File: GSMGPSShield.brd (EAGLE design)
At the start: 68.6 x 53.3 mm, 65 parts, among them IC1 RT8289, IC2 SIM900, J1 SIM Socket, J2 Antenna, J3 Breakout 1, J4 Breakout 2, J5 ARDUINO-SHIELD_R3, Q1 2N7002, Q2 2N7002, Q3 2N7002, Q4 2N7002, Q5 2N7002

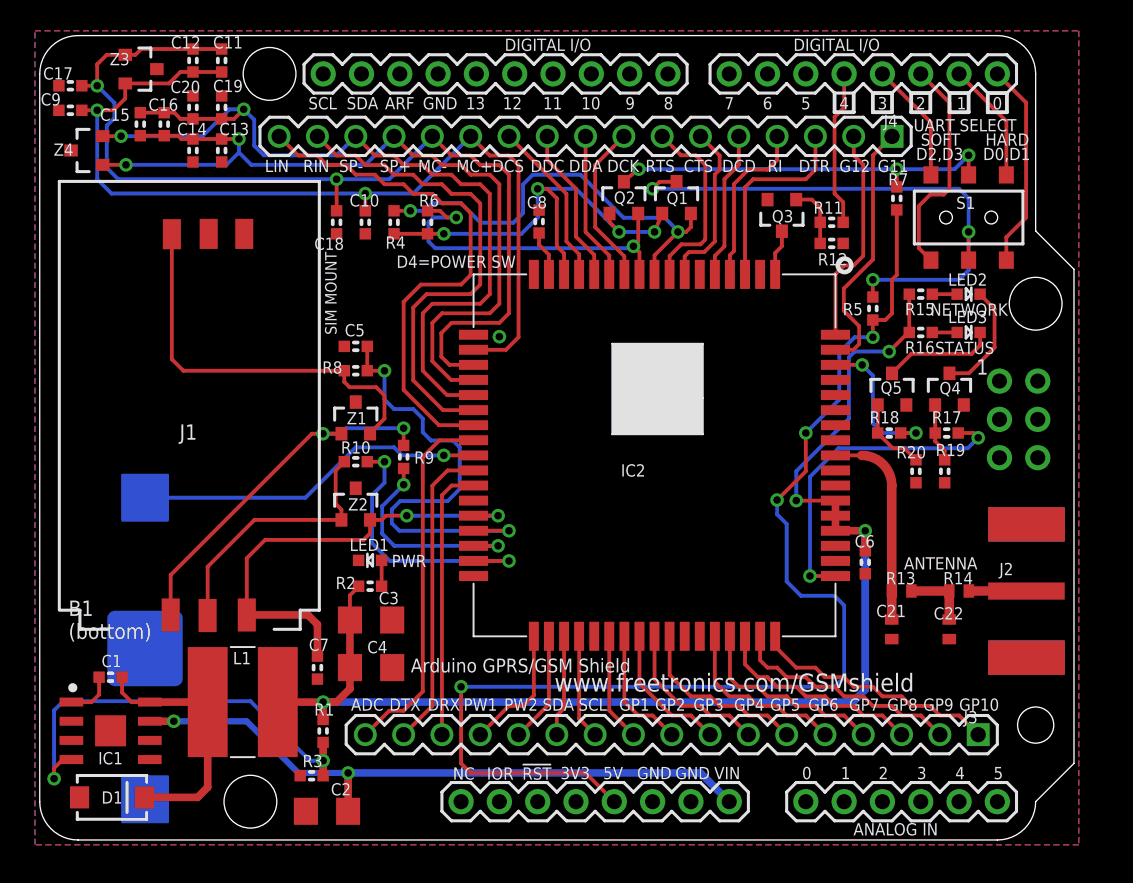
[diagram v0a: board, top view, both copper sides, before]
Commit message: changed to SIM908 module, first finished draft
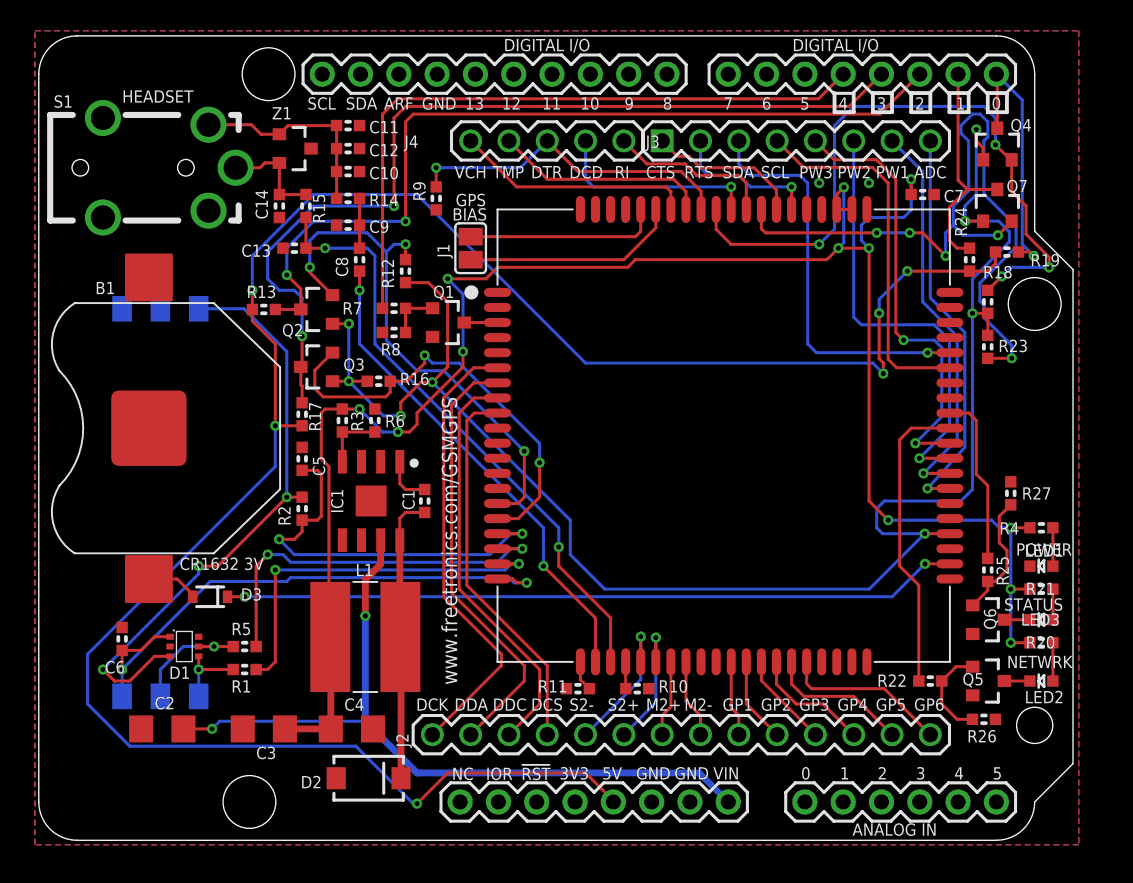
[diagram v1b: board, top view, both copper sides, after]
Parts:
- removed C15, C17, C19: 10pF, freetronics-master-v1:0603
- removed C16, C18, C20: 33pF, freetronics-master-v1:0603
- removed C21, C22: NOT PLACED, freetronics-master-v1:C0402
- removed Z2, Z3, Z4: PGB102ST23, freetronics-luke:SOT23-3
- added D2: B340A-13-F, freetronics-luke:SMA
- added D3: NSR0340HT1G, freetronics-luke:SOD-323
- added IC3: SIM908, freetronics-luke:SIM908
- added Q6, Q7: 2N7002, freetronics-luke:SOT23-3
- added R21: 1K, freetronics-master-v1:0603
- added R22, R25: 10R, freetronics-master-v1:0603
- added R23, R24: 10K, freetronics-master-v1:0603
- added R26, R27: 100K, freetronics-master-v1:0603
- C11, C13, C9: value 10pF -> 33pF
- C12: value 33pF -> 10pF
- C8: value 100nF -> 1µF
- D1: value B340A-13-F -> SMF05CT1G; device freetronics-luke:SMA -> freetronics-luke:SC70-6
- IC2: value SIM900 -> C70710M0065002; device ICs_v54:SIM900 -> freetronics-luke:C70710M0065002
- J1: value SIM Socket -> Active GPS Antenna Bias; device SparkFun2:SIMHOLDER3 -> freetronics-luke:SJ
- J2: value Antenna -> (none); device con-coax:J502-ND-142-0701-881/886 -> freetronics-master-v1:1X14
- J3: value Breakout 1 -> (none); device freetronics-master-v1:1X17 -> freetronics-master-v1:1X08
- J4: value Breakout 2 -> (none); device freetronics-master-v1:1X17 -> freetronics-master-v1:1X05
- J5: value ARDUINO-SHIELD_R3 -> ARDUINO-SHIELD_R3_NOISP; device freetronics-luke:ARDUINO-SHIELD_R3 -> freetronics-luke:ARDUINO-SHIELD_R3_NOISP
- R1: value 27K -> 22R
- R10: value 22R -> 0Ω
- R11: value 10R -> 0Ω
- R12, R19: value 100K -> 10K
- R13: value 0R -> 10K; device freetronics-master-v1:C0402 -> freetronics-master-v1:0603
- R14: value 0R -> 10Ω; device freetronics-master-v1:C0402 -> freetronics-master-v1:0603
- R15: value 1K -> 68Ω
- R16: value 1K -> 10K
- R17, R18: value 10R -> 10K
- R2: value 1K -> 22R
- R20: value 100K -> 1K
- R3: value 12K -> 51kΩ 1%
- R4: value 10K -> 1kΩ
- R5: value 10K -> 22R
- R6: value 10K -> 22kΩ 1%
- R7: value 10K -> 10R
- R8: value 22R -> 100K
- R9: value 22R -> 10K
- S1: value UART Select -> 4UCON-18899; device freetronics-master-v1:AYZ0202 -> freetronics-jon:4UCON-18899
- moved S1 57.5 mm to (4.83, 45.2), turned to 0 degrees
- moved C7 50.9 mm to (59.2, 43.4), turned to 180 degrees
- moved C6 49.5 mm to (6.10, 14.0), turned to 270 degrees
- moved R14 48.2 mm to (21.1, 43.2), turned to 180 degrees
- moved R4 47.5 mm to (67.1, 21.3), turned to 0 degrees
- moved R5 47.3 mm to (14.2, 13.5), turned to 0 degrees
- moved R13 46.2 mm to (15.5, 35.8)
- moved J3 44.6 mm to (41.9, 47.0), turned to 0 degrees
- moved LED1 44.5 mm to (67.1, 18.8)
- moved R17 42.8 mm to (18.0, 28.9), turned to 90 degrees
- moved R15 41.2 mm to (18.3, 42.7), turned to 90 degrees
- moved J2 38.0 mm to (26.7, 7.62)
- moved IC2 36.5 mm to (8.64, 10.2), flipped to the bottom, turned to 90 degrees
- moved R16 36.1 mm to (23.1, 31.1)
- moved R11 35.2 mm to (36.3, 10.7), turned to 180 degrees
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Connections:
- removed net !GSM_RESET: C8.2, IC2.16
- removed net DBG_RXD: IC2.28, J3.15
- removed net DBG_TXD: IC2.27, J3.16
- removed net DISP_DC: IC2.13, J4.10
- removed net GPIO10: IC2.51, J3.1
- removed net GPIO11: IC2.67, J4.1
- removed net GPIO12: IC2.68, J4.2
- removed net GPIO7: IC2.48, J3.4
- removed net GPIO8: IC2.49, J3.3
- removed net GPIO9: IC2.50, J3.2
- removed net LIN_L: IC2.24, J4.17
- removed net LIN_R: IC2.23, J4.16
- removed net MIC+: C10.2, C11.2, C12.2, C9.2, IC2.19, J4.12, Z3.2
- removed net MIC-: C11.1, C12.1, C17.2, C18.2, IC2.20, J4.13, Z3.1
- removed net N$22: J1.2, R10.2, Z2.1
- removed net N$40: J1.3, R9.2, Z1.1
- removed net N$49: J1.4, R8.2, Z1.2
- removed net N$6: B1.PWR@1, IC2.26
- removed net N$67: IC2.1, Q3.3
- removed net N$69: Q3.1, R11.1, R12.2
- removed net N$70: C22.2, R13.2, R14.1
- removed net N$71: J2.1, R14.2
- removed net RF_ANT: C21.2, IC2.60, R13.1
- removed net RXD_5V: Q2.3, R7.2, S1.5
- removed net SPK+: C13.2, C14.2, C15.2, C16.2, IC2.21, J4.14, Z4.1
- removed net SPK-: C15.1, C16.1, C19.2, C20.2, IC2.22, J4.15, Z4.2
- removed net TXD_5V: Q1.3, R5.2, S1.2
- new net DISP_D/C: IC3.8, J2.3
- new net GPS_RXD: IC3.16, Q3.2, R16.2
- new net GPS_TXD: IC3.15, Q2.2, R12.2
- new net MIC1+: C13.2, IC3.23, R15.1
- new net MIC2+: IC3.27, J2.7
- new net MIC2-: IC3.28, J2.8
- new net N$10: IC3.21, R11.1
- new net N$11: IC3.24, R10.1
- new net N$12: D1.5, IC2.2, R5.1
- new net N$13: D1.4, IC2.3, R1.1
- new net N$15: D1.3, IC2.6, R2.1
- new net N$16: C14.2, R15.2, S1.1, Z1.2
- new net N$17: C10.2, C11.2, C12.2, R14.2, S1.3, Z1.1
- new net N$20: C8.1, C9.2, R14.1
- new net N$34: Q1.1, R7.1, R8.2
- new net N$7: D3.K, IC3.42
- new net N$8: IC3.3, Q1.3
- new net N$9: B1.PWR@1, D3.A
- new net PWM3: IC3.50, J3.5
- new net SPK1+: C8.2, IC3.22
- new net SPK2+: IC3.26, J2.6
- new net SPK2-: IC3.25, J2.5
- new net TEMP_BAT: IC3.73, J4.2
- new net VANT_IN: IC3.76, J1.2
- new net VANT_OUT: IC3.75, J1.1
- new net V_CHG: IC3.74, J4.1
- net +2.8V: now also IC3.44, Q3.1, Q4.1, Q7.1, R12.1, R16.1, R18.1, R23.1; no longer IC2.15, Q1.1, R4.1, R6.1
- net +4.0V: now also C7.2, IC3.62, IC3.63, R20.1, R21.1, R3.1, R4.1; no longer C6.2, IC2.55, IC2.56, IC2.57, R1.1, R15.1, R16.1, R2.1
- net +5V: now also R13.1, R17.1, R19.1, R24.1; no longer R5.1, R7.1
- net ADC: now also IC3.47, J3.8; no longer IC2.25, J3.17
- net CTS: now also IC3.67, J3.1; no longer IC2.7, J4.6
- net D0: now also Q4.3, R19.2; no longer S1.1
- net D1: now also Q7.3, R24.2; no longer S1.4
- net D2: now also Q2.3, R13.2; no longer S1.3
- net D3: now also Q3.3, R17.2; no longer S1.6
- net DCD: now also IC3.70, J4.4; no longer IC2.5, J4.5
- net DISP_CLK: now also IC3.6, J2.1; no longer IC2.11, J4.8
- net DISP_CS: now also IC3.9, J2.4; no longer IC2.14, J4.11
- net DISP_DATA: now also IC3.7, J2.2; no longer IC2.12, J4.9
- net DTR: now also IC3.72, R9.1; no longer IC2.3
- net GND: now also C11.1, C12.1, D1.2, D2.A, IC2.4, IC3.1, IC3.10, IC3.14, IC3.2, IC3.37, IC3.40, IC3.41, IC3.43, IC3.5, IC3.57, IC3.58, IC3.60, IC3.61, IC3.64, IC3.65, IC3.77, IC3.78, IC3.80, Q1.2, Q6.2, R10.2, R11.2, R26.1, R27.1, R6.1, R8.1, R9.2, S1.4; no longer C17.1, C18.1, C19.1, C20.1, C21.1, C22.1, C8.1, D1.A, IC2.17, IC2.18, IC2.29, IC2.39, IC2.45, IC2.46, IC2.53, IC2.54, IC2.58, IC2.59, IC2.61, IC2.62, IC2.63, IC2.64, IC2.65, J1.6, J2.G@1, J2.G@2, J2.G@3, J2.G@4, J5.GND@2, Q3.2, Q4.2, R12.1, R19.1, R20.1, R3.1, Z2.3, Z3.3, Z4.3
- net GPIO1: now also IC3.31, J2.9; no longer IC2.40, J3.10
- net GPIO2: now also IC3.32, J2.10; no longer IC2.41, J3.9
- net GPIO3: now also IC3.33, J2.11; no longer IC2.42, J3.8
- net GPIO4: now also IC3.34, J2.12; no longer IC2.43, J3.7
- net GPIO5: now also IC3.35, J2.13; no longer IC2.44, J3.6
- net GPIO6: now also IC3.36, J2.14; no longer IC2.47, J3.5
- net N$1: now also R4.2; no longer R2.2
- net N$143: now also D2.K; no longer D1.K
- net N$144: now also R6.2; no longer R1.2
- net N$2: now also Q5.3; no longer Q4.3
- net N$3: now also Q6.3; no longer Q5.3
- net N$4: now also Q5.1, R22.1, R26.2; no longer Q4.1, R17.1, R19.2
- net N$5: now also Q6.1, R25.1, R27.2; no longer Q5.1, R18.1, R20.2
- net N$76: now also R21.2; no longer R16.2
- net N$77: now also R20.2; no longer R15.2
- net NETWORK_LED: now also IC3.51, R22.2; no longer IC2.52, R17.2
- net POWER_ON: now also R7.2; no longer R11.2
- net PWM1: now also IC3.48, J3.7; no longer IC2.35, J3.14
- net PWM2: now also IC3.49, J3.6; no longer IC2.36, J3.13
- net RI: now also IC3.69, J4.5; no longer IC2.4, J4.4
- net RTS: now also IC3.66, J3.2; no longer IC2.8, J4.7
- net RXD: now also IC3.68, Q7.2, R23.2; no longer IC2.10, Q2.2, R6.2
- net SCL: now also IC3.55, J3.4; no longer IC2.38, J3.11
- net SDA: now also IC3.56, J3.3; no longer IC2.37, J3.12
- net SIM_CLK: now also IC3.19, R1.2; no longer IC2.32, R9.1
- net SIM_DATA: now also IC3.17, R2.2; no longer IC2.31, R8.1
- net SIM_RST: now also IC3.18, R5.2; no longer IC2.33, R10.1
- net SIM_VDD: now also C6.2, D1.1, IC2.1, IC3.20; no longer C7.2, IC2.30, J1.1, Z2.2
- net STATUS_LED: now also IC3.52, R25.2; no longer IC2.66, R18.2
- net TXD: now also IC3.71, Q4.2, R18.2; no longer IC2.9, Q1.2, R4.2
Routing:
- net +2.8V: track 30.4 -> 112.2 mm, vias 4 -> 8
- net MIC-: track 66.7 -> 0.00 mm, vias 2 -> 0
- net MIC+: track 62.1 -> 0.00 mm, vias 2 -> 0
- net +5V: track 80.6 -> 139.6 mm, vias 4 -> 6
- net SPK-: track 57.5 -> 0.00 mm, vias 2 -> 0
- net SPK+: track 55.3 -> 0.00 mm, vias 2 -> 0
- net D3: track 8.03 -> 60.6 mm, vias 0 -> 2
- net N$7: track 0.00 -> 48.8 mm, vias 0 -> 2
- net D2: track 14.8 -> 56.8 mm, vias 0 -> 2
- net N$15: track 0.00 -> 40.4 mm, vias 0 -> 3
- net MIC1+: track 0.00 -> 40.2 mm, vias 0 -> 2
- net +4.0V: track 86.2 -> 125.7 mm, vias 4 -> 12
- net TXD_5V: track 37.4 -> 0.00 mm, vias 3 -> 0
- net GPS_TXD: track 0.00 -> 35.6 mm, vias 0 -> 3
- net LIN_L: track 35.5 -> 0.00 mm
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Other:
- board text added: "2.4V logic on all spare SIM908 breakout pins!"
- board text added: "B1"
- board text added: "BIAS"
- board text added: "CR1632 3V"
- board text added: "D0 D1 = GSM UART"
- board text added: "D2 D3 = GPS UART"
- board text added: "D4 = POWER SW"
- board text added: "GPS"
- board text added: "GSM/GPS Shield for Arduino"
- board text added: "HEADSET"
- board text added: "M2+"
- board text added: "M2-"
- board text added: "NETWRK"
- board text added: "POWER"
- board text added: "PW3"
- board text added: "S2+"
- board text added: "S2-"
- board text added: "SIM CARD"
- board text added: "TMP"
- board text added: "VCH"
- board text added: "www.freetronics.com/GSMGPS"
- board text added: "www.freetronics.com/gsmgps"
- board text removed: "1"
- board text removed: "A"
- board text removed: "ANTENNA"
- board text removed: "Arduino GPRS/GSM Shield"
- board text removed: "B1 (bottom)"
- board text removed: "D0,D1"
- board text removed: "D2,D3"
- board text removed: "D4=POWER SW"
- board text removed: "DRX"
- board text removed: "DTX"
- board text removed: "G11"
- board text removed: "G12"
- board text removed: "GP10"
- board text removed: "GP7"
- board text removed: "GP8"
- board text removed: "GP9"
- board text removed: "GSM/GPRS Shield for Arduino"
- board text removed: "HARD"
- board text removed: "J1"
- board text removed: "K"
- board text removed: "LIN"
- board text removed: "MC+"
- board text removed: "MC-"
- board text removed: "NETWORK"
- board text removed: "PWR"
- board text removed: "RIN"
- board text removed: "SIM MOUNT"
- board text removed: "SOFT"
- board text removed: "SP+"
- board text removed: "SP-"
- board text removed: "UART SELECT"
- board text removed: "www.freetronics.com/GSMshield"
- board text removed: "www.freetronics.com/gsm"

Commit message: Relocated project close to 0,0 origin. Couldn't get it quite right
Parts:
- C8: value 1µF -> 1uF
- R10, R11: value 0Ω -> 0R
- R14: value 10Ω -> 10R
- R15: value 68Ω -> 68R
- R3: value 51kΩ 1% -> 51K 1%
- R4: value 1kΩ -> 1K
- R6: value 22kΩ 1% -> 22K 1%
- moved S1 0.84 mm to (4.26, 44.6)
- moved C7 0.84 mm to (58.6, 42.8)
- moved J5 0.84 mm to (33.0, 26.7)
- moved Q4 0.84 mm to (63.6, 46.1)
- moved Q7 0.84 mm to (63.6, 42.1)
- moved R11 0.84 mm to (35.8, 10.1)
- moved R26 0.84 mm to (62.7, 8.02)
- moved R27 0.84 mm to (64.5, 23.0)
- moved B1 0.84 mm to (7.31, 27.3)
- moved J2 0.84 mm to (26.1, 7.00)
- moved C5 0.84 mm to (17.5, 25.3)
- moved R2 0.84 mm to (17.5, 22.0)
- moved R25 0.84 mm to (62.9, 17.9)
- moved C6 0.84 mm to (5.53, 13.4)
- moved R1 0.84 mm to (13.7, 11.3)
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
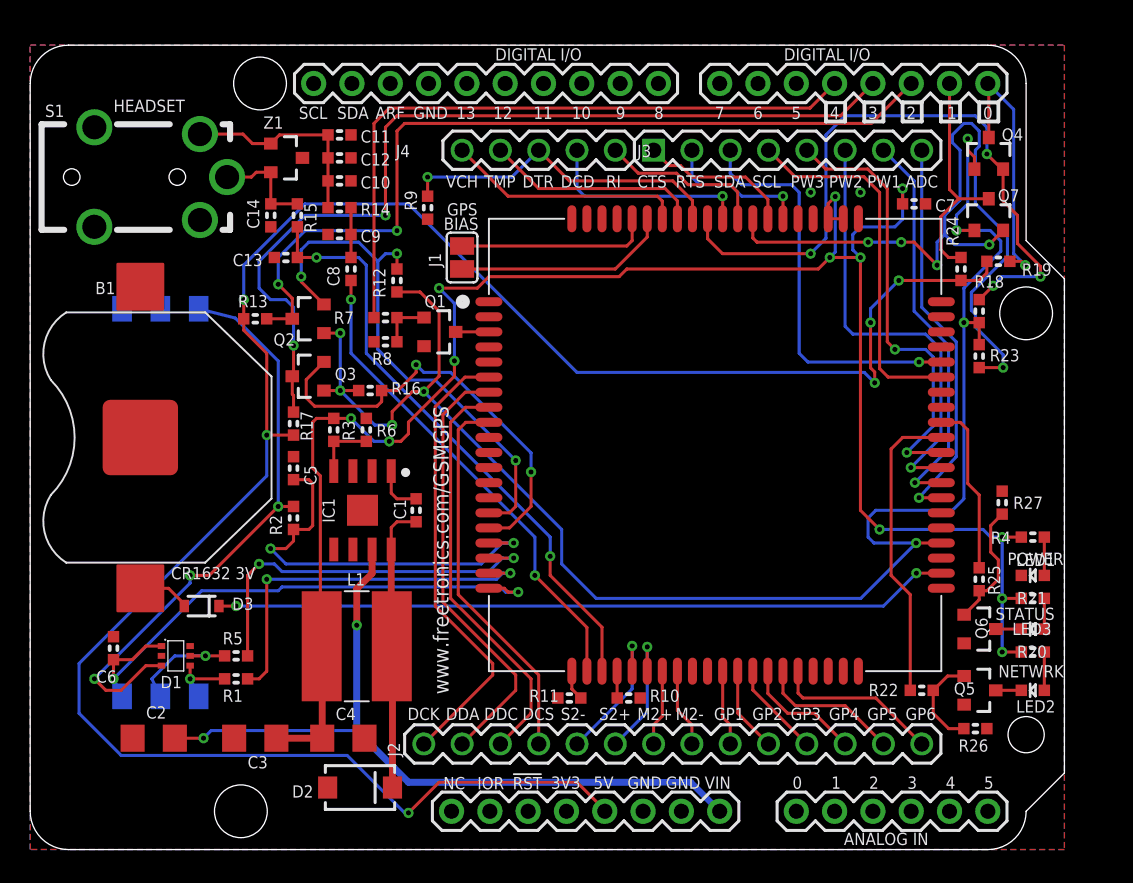
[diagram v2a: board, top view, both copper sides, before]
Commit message: Fixed footprint for headphone socket Changed pin assignments to D2-D6 to clear D0/D1 UART for programming Added ICSP header for pass-through Replaced level shifter FETs with RJU003N03 Added orientation markers in tinfo layer for assembler Changed labels to vector and increased sizes
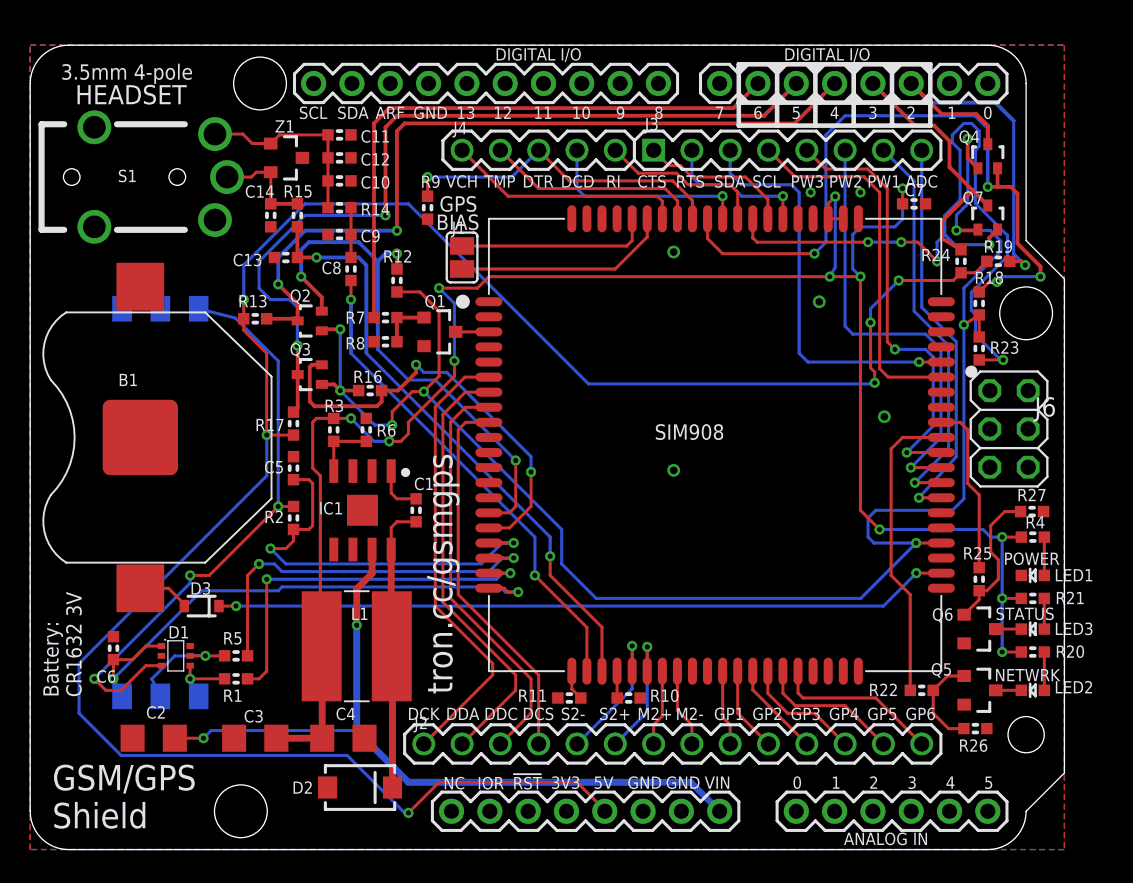
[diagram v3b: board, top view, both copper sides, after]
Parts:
- added J6: ICSPPTH, freetronics-jon:2X03PTH
- Q2, Q3, Q4, Q7: value 2N7002 -> RJU003N03 N-MOSFET; device freetronics-luke:SOT23-3 -> freetronics-jon:SOT32-3
- moved R27 2.07 mm to (66.4, 22.4), turned to 180 degrees
- moved R23 0.51 mm to (62.9, 33.2)
- moved R24 0.51 mm to (61.7, 39.0)
- moved R18 0.51 mm to (62.9, 36.2)
- moved Q4 0.16 mm to (63.5, 46.0)
- moved Q7 0.16 mm to (63.5, 41.9)
- moved Q2 0.16 mm to (18.5, 35.1)
- moved Q3 0.13 mm to (18.5, 31.5)
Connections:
- removed net D0: J5.D0, Q4.3, R19.2
- removed net D1: J5.D1, Q7.3, R24.2
- removed net POWER_ON: J5.D4, R7.2
- new net D4: J5.D4, Q2.3, R13.2
- new net D5: J5.D5, Q3.3, R17.2
- new net D6: J5.D6, R7.2
- net D2: now also Q4.3, R19.2; no longer Q2.3, R13.2
- net D3: now also Q7.3, R24.2; no longer Q3.3, R17.2
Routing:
- net D5: track 0.00 -> 55.8 mm, vias 0 -> 2
- net D4: track 0.00 -> 52.5 mm, vias 0 -> 2
- net POWER_ON: track 44.5 -> 0.00 mm
- net D3: track 60.6 -> 17.5 mm, vias 2 -> 0
- net D6: track 0.00 -> 39.4 mm
- net D2: track 56.8 -> 26.3 mm, vias 2 -> 1
- net D0: track 17.8 -> 0.00 mm, vias 1 -> 0
- net D1: track 15.3 -> 0.00 mm
- net TXD: track 44.5 -> 46.5 mm
- net N$5: track 8.43 -> 9.73 mm
- net +2.8V: track 112.2 -> 113.5 mm
- net N$17: track 13.8 -> 12.8 mm
- net +4.0V: track 125.7 -> 126.4 mm
- net RXD: track 50.7 -> 50.0 mm
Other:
- board text added: "3.5mm 4-pole"
- board text added: "A"
- board text added: "Battery: CR1632 3V"
- board text added: "Copyright 2014 Freetronics Pty Ltd Released under the terms of the TAPR Open Hardware License www.tapr.org/ohl"
- board text added: "D2: GSM RX D3: GSM TX D4: GPS RX D5: GPS TX D6: Power"
- board text added: "GSM/GPS Shield"
- board text added: "K"
- board text added: "SIM908"
- board text added: "tron.cc/gsmgps"
- board text added: "v1.0 SKU: GSMGPS"
- board text removed: "CR1632 3V"
- board text removed: "Copyright 2013 Freetronics Pty Ltd Released under the terms of the TAPR Open Hardware License www.tapr.org/ohl"
- board text removed: "D0 D1 = GSM UART"
- board text removed: "D2 D3 = GPS UART"
- board text removed: "D4 = POWER SW"
- board text removed: "v1.0 SKU: GSM"
- board text removed: "www.freetronics.com/GSMGPS"
